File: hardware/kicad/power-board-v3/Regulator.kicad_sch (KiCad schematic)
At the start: 58 parts

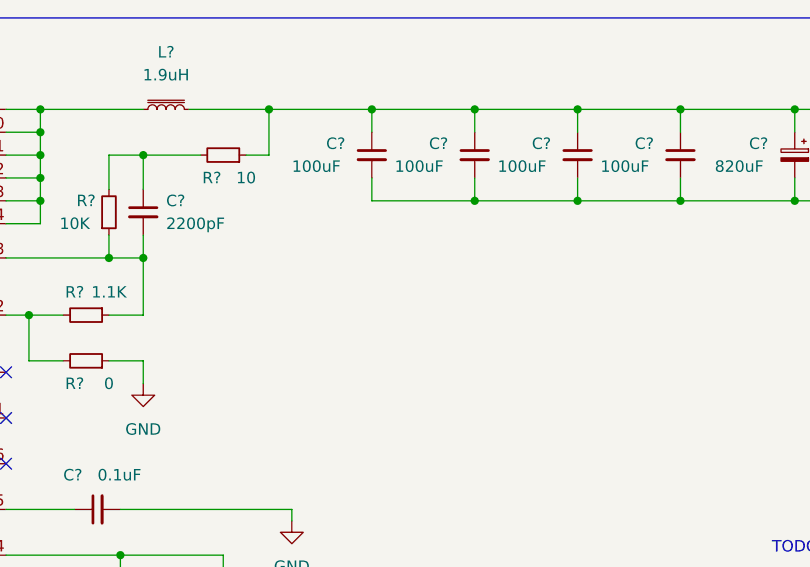
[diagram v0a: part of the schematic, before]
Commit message: add base symbol and wiring
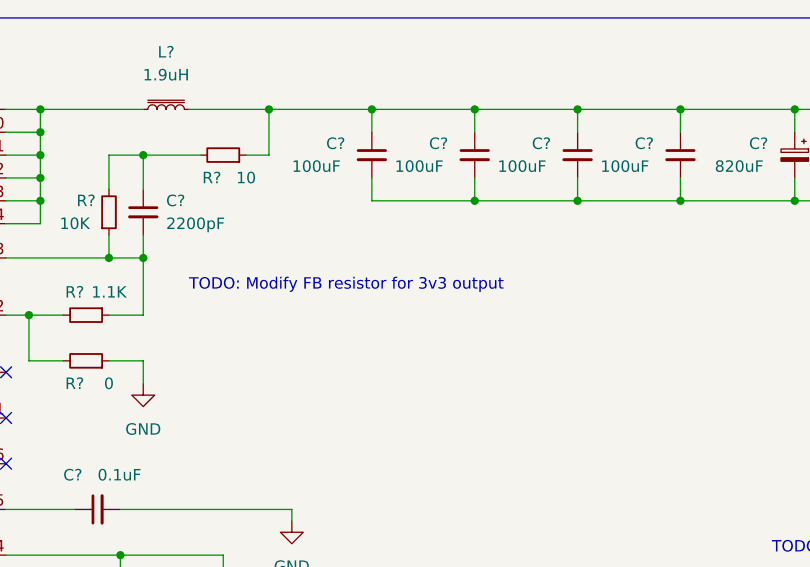
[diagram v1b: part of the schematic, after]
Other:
- note added: "TODO: Modify FB resistor for 3v3 output"
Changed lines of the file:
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@@
   )
   (polyline (pts (xy 11.43 105.41) (xy 284.48 105.41))
-    (stroke (width 0) (type default) (color 0 0 0 0))
+    (stroke (width 0) (type solid) (color 0 0 0 0))
   )
   (wire (pts (xy 240.03 30.48) (xy 240.03 33.02))
@@
     (stroke (width 0) (type default) (color 0 0 0 0))
   )
+  (text "TODO: Modify FB resistor for 3v3 output" (at 156.21 135.89 0)
+    (effects (font (size 1.27 1.27)) (justify left bottom))
+  )
   (text "TODO: Verify regulator's inductor and capacitor value and size"
